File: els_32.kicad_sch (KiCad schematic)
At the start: 53 parts, among them J1 HR911105A, J2 JST-XH, J3 JST-XH, J4 Conn_01x03_Female, J5 WAGO, Q1 2N7002, Q2 Q_PMOS_DGS, U1 LAN8720A, U2 ESP32-WROOM-E, U3 MP2307, U4 LM3940

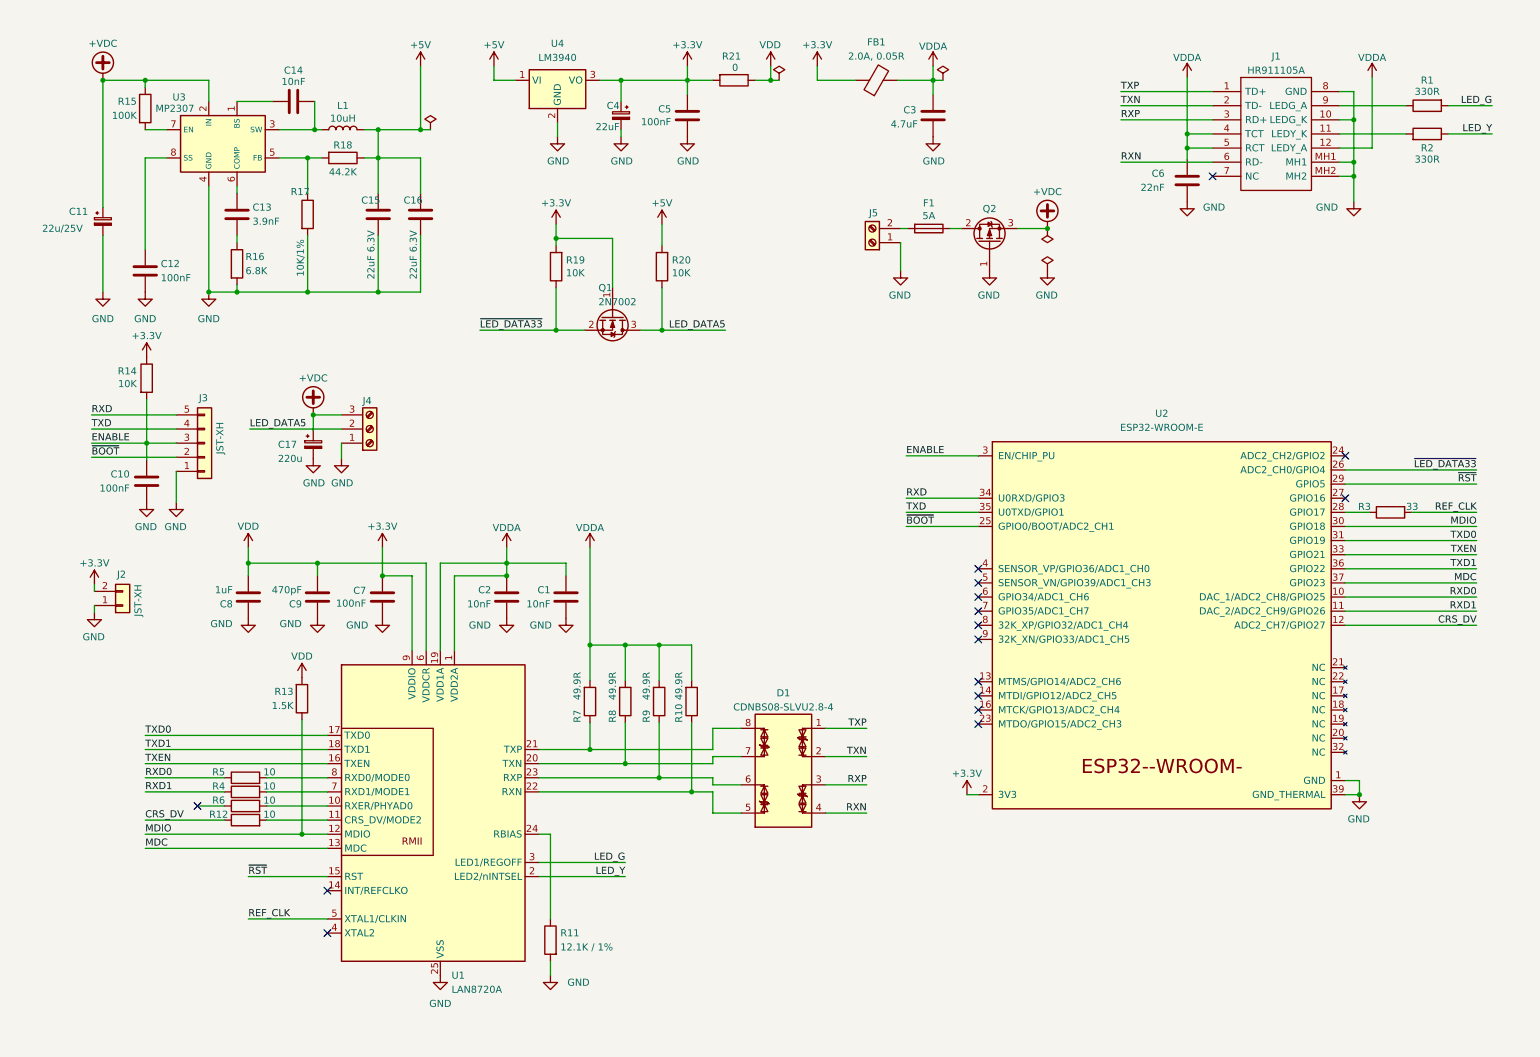
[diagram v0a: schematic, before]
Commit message: Update schematic: v0.2
- use TPS54321 for VDC -> 3.3V
- use 5.6 zener for level-shifting
- cleanup
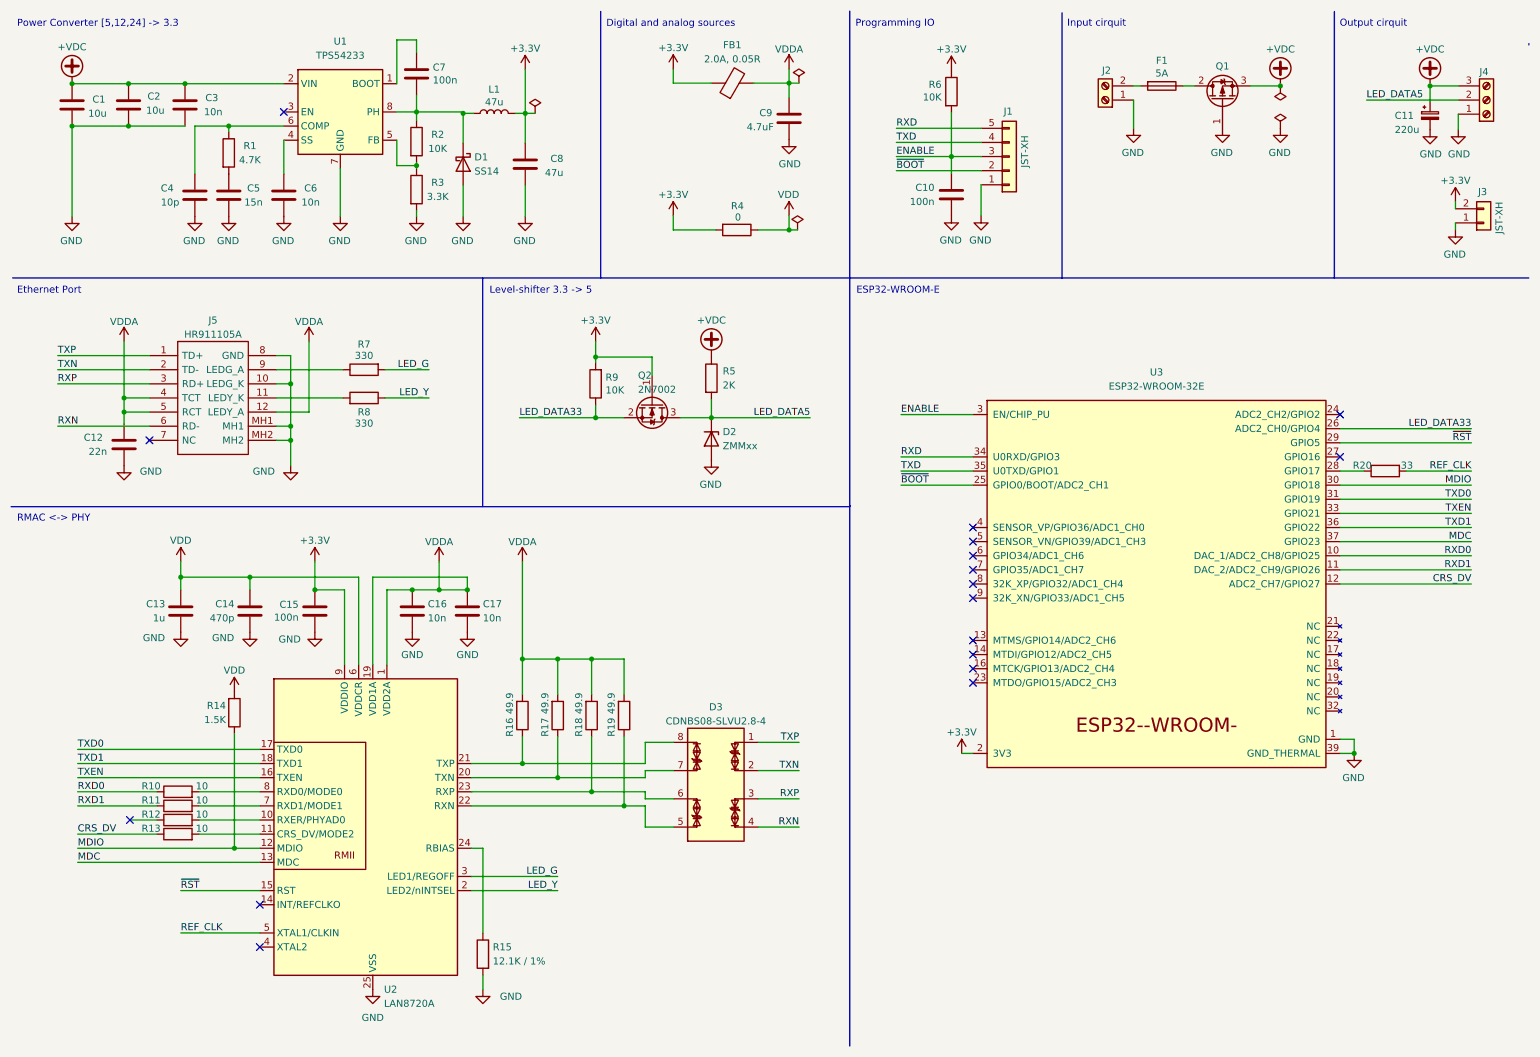
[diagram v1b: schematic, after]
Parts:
- removed C11: 22u/25V, Capacitor_SMD:C_0805_2012Metric, symbol Device:C_Polarized_Small
- removed C12: 100nF, Capacitor_SMD:C_0402_1005Metric, symbol Device:C
- removed C13: 3.9nF, Capacitor_SMD:C_0402_1005Metric, symbol Device:C
- removed C14: 10nF, Capacitor_SMD:C_0402_1005Metric, symbol Device:C
- removed C15, C16: 22uF 6.3V, Capacitor_SMD:C_0603_1608Metric, symbol Device:C
- removed C4: 22uF, Capacitor_Tantalum_SMD:CP_EIA-3528-21_Kemet-B, symbol Device:C_Polarized_Small
- removed R15: 100K, Resistor_SMD:R_0402_1005Metric, symbol Device:R
- removed R16: 6.8K, Resistor_SMD:R_0402_1005Metric, symbol Device:R
- removed R17: 10K/1%, Resistor_SMD:R_0402_1005Metric, symbol Device:R
- removed R18: 44.2K, Resistor_SMD:R_0402_1005Metric, symbol Device:R
- removed R20: 10K, Resistor_SMD:R_0402_1005Metric, symbol Device:R
- removed U3: MP2307, Package_SO:SOIC-8-1EP_3.9x4.9mm_P1.27mm_EP2.62x3.51mm, symbol MP2307:MP2307
- removed U4: LM3940, Package_TO_SOT_SMD:SOT-223-3_TabPin2, symbol LM3940:LM3940
- added C1, C2: 10u, Capacitor_SMD:C_1206_3216Metric, symbol Device:C
- added C3, C6: 10n, Capacitor_SMD:C_0402_1005Metric, symbol Device:C
- added C4: 10p, Capacitor_SMD:C_0603_1608Metric, symbol Device:C
- added C7: 100n, Capacitor_SMD:C_0402_1005Metric, symbol Device:C
- added C8: 47u, Capacitor_SMD:C_1206_3216Metric, symbol Device:C
- added D1: SS14, Diode_SMD:D_SMA, symbol Device:D_Schottky
- added D2: ZMMxx, Diode_SMD:D_MiniMELF, symbol Diode:ZMMxx
- added R1: 4.7K, Resistor_SMD:R_0402_1005Metric, symbol Device:R
- added R2: 10K, Resistor_SMD:R_0402_1005Metric, symbol Device:R
- added R3: 3.3K, Resistor_SMD:R_0402_1005Metric, symbol Device:R
- added R5: 2K, Resistor_SMD:R_1206_3216Metric, symbol Device:R
- added U1: TPS54233, Package_SO:SOIC-8_3.9x4.9mm_P1.27mm, symbol Regulator_Switching:TPS54233
- C10: value 100nF -> 100n
- C12: renamed from C6; value 22nF -> 22n
- C13: renamed from C8; value 1uF -> 1u
- C14: renamed from C9; value 470pF -> 470p
- C15: renamed from C7; value 100nF -> 100n
- C16: renamed from C2; value 10nF -> 10n
- C17: renamed from C1; value 10nF -> 10n
- C5: value 100nF -> 15n; footprint Capacitor_SMD:C_0402_1005Metric -> Capacitor_SMD:C_0603_1608Metric; LCSC C307331 -> C1596
- L1: value 10uH -> 47u; footprint Inductor_SMD:L_Sunlord_MWSA0518_5.4x5.2mm -> Inductor_SMD:L_Sunlord_MWSA06xxS; LCSC C181721 -> C408471
- R16: renamed from R7; value 49.9R -> 49.9
- R17: renamed from R8; value 49.9R -> 49.9
- R18: renamed from R9; value 49.9R -> 49.9
- R19: renamed from R10; value 49.9R -> 49.9
- R7: renamed from R1; value 330R -> 330
- R8: renamed from R2; value 330R -> 330
- U3: renamed from U2; value ESP32-WROOM-E -> ESP32-WROOM-32E; footprint Espressif:ESP32-WROOM-32E -> els_32-libs:ESP32-WROOM-32E
- renumbered C17 to C11, C3 to C9, D1 to D3, J3 to J1, J5 to J2, J2 to J3, J1 to J5, Q2 to Q1, Q1 to Q2, R5 to R10, R4 to R11, R6 to R12, R12 to R13, R13 to R14, R11 to R15, R3 to R20, R21 to R4, R14 to R6, R19 to R9, U1 to U2
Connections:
- net +5V is gone; now on net +3.3V: L1.2
- net +3.3V: now also C8.2; no longer C5.1
- net +VDC: now also C1.2, C2.1, C3.2, R5.1, U1.2 (VIN)
- net GND: now also C13.2, C14.2, C1.1, C2.2, C3.1, C4.1, C6.1, C8.1, D1.2 (A), D2.2 (A), R3.2, U1.7 (GND); no longer C13.1, C14.1
- net LED_DATA5: now also D2.1 (K), R5.2
- net VDD: now also C13.1, C14.1; no longer C13.2, C14.2
- net at L1.1: now also C7.2, D1.1 (K), R2.1, U1.8 (PH)
- net ~{LED_DATA33} renamed LED_DATA33
- new net: C4.2, R1.1, U1.6 (COMP)
- new net: R2.2, R3.1, U1.5 (FB)
- new net: C6.2, U1.4 (SS)
- new net: C5.1, R1.2
- new net: C7.1, U1.1 (BOOT)
- no-connect marks 16 -> 17
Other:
- note added: "Digital and analog sources"
- note added: "ESP32-WROOM-E"
- note added: "Ethernet Port"
- note added: "Input cirquit"
- note added: "Level-shifter 3.3 -> 5"
- note added: "Output cirquit"
- note added: "Power Converter [5,12,24] -> 3.3"
- note added: "Programming IO"
- note added: "RMAC <-> PHY"
- title: (none) -> ELS-32
- moved on the sheet: C10, C11, C12, C13, C14, C15, C16, C17, C9, D3, F1, FB1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

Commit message: update save
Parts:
- removed D2: ZMMxx, Diode_SMD:D_MiniMELF, symbol Diode:ZMMxx
- removed D3: CDNBS08-SLVU2.8-4, Package_SO:SOIC-8_3.9x4.9mm_P1.27mm, symbol Power_Protection:CDNBS08-SLVU2.8-4
- removed Q2: 2N7002, Package_TO_SOT_SMD:SOT-23, symbol Transistor_FET:BSS138
- removed R4: 0, Resistor_SMD:R_1206_3216Metric, symbol Device:R
- removed U3: ESP32-WROOM-32E, els_32-libs:ESP32-WROOM-32E, symbol Espressif:ESP32-WROOM-E
- added AE1: PCB_Ant, els_32-libs:ESPRESSIF_ESP32_MIFA_2.4GHz_Right, symbol PCB_ant:PCB_Ant
- added C12: 22u, Capacitor_SMD:C_1206_3216Metric, symbol Device:C
- added C13, C14, C23, C24, C28, C31, C32, C34, C35: 100n, Capacitor_SMD:C_0402_1005Metric, symbol Device:C
- added C21, C22: TBD, Capacitor_SMD:C_0402_1005Metric, symbol Device:C
- added C25: 10n, Capacitor_SMD:C_0402_1005Metric, symbol Device:C
- added C26, C27: 27p, Capacitor_SMD:C_0402_1005Metric, symbol Device:C
- added C29: 100p, Capacitor_SMD:C_0402_1005Metric, symbol Device:C
- added C30, C33: 1u, Capacitor_SMD:C_0402_1005Metric, symbol Device:C
- added C36: 10u, Capacitor_SMD:C_0603_1608Metric, symbol Device:C
- added D2, D3, D4, D5: ESD5Z5CL, Diode_SMD:D_SOD-523, symbol Device:D_TVS
- added L2: TBD, Inductor_SMD:L_0402_1005Metric, symbol Device:L
- added L3: 2n, Inductor_SMD:L_0402_1005Metric, symbol Device:L
- added R11: 2K, Resistor_SMD:R_0402_1005Metric, symbol Device:R
- added R12, R14: 33, Resistor_SMD:R_0402_1005Metric, symbol Device:R
- added R26, R27: 10, Resistor_SMD:R_0402_1005Metric, symbol Device:R
- added R28, R29: 4.7K, Resistor_SMD:R_0402_1005Metric, symbol Device:R
- added R30, R32, R6, R7, R8: 10K, Resistor_SMD:R_0402_1005Metric, symbol Device:R
- added R31: 10m, Resistor_SMD:R_1206_3216Metric, symbol Device:R_Shunt
- added R33: 510, Resistor_SMD:R_0402_1005Metric, symbol Device:R_Small
- added SW1, SW2: SW_MEC_5E, els_32-libs:TS1187ABAB, symbol Switch:SW_MEC_5E
- added U2: AZ1117-3.3, Package_TO_SOT_SMD:SOT-223-3_TabPin2, symbol Regulator_Linear:AZ1117-3.3
- added U3: SN74LVC2T45DCUR, Package_SO:VSSOP-8_2.4x2.1mm_P0.5mm, symbol Logic_LevelTranslator:SN74LVC2T45DCUR
- added U4: ESP32-D0WD-V3, Package_DFN_QFN:QFN-48-1EP_5x5mm_P0.35mm_EP3.7x3.7mm, symbol ESP32-D0WD-V3:ESP32-D0WD-V3
- added U6: INA226AIDGSR, Package_SO:MSOP-10_3x3mm_P0.5mm, symbol INA226AIDGSR:INA226AIDGSR
- added U7: W25Q32JVSS, Package_SO:SOIC-8_5.23x5.23mm_P1.27mm, symbol Memory_Flash:W25Q32JVSS
- added Y1: Crystal_GND24, Crystal:Crystal_SMD_2520-4Pin_2.5x2.0mm, symbol Device:Crystal_GND24
- C5: renamed from C9; value 4.7uF -> 4.7u
- F1: value 5A -> 10A
- J1: renamed from J2; value WAGO -> Conn_01x02_Female; footprint TerminalBlock_WAGO:TerminalBlock_WAGO_236-102_1x02_P5.00mm_45Degree -> els_32-libs:DBT50G-7.62-2P; LCSC (none) -> C496127
- J2: renamed from J4; value Conn_01x03_Female -> Conn_01x04_Female; footprint TerminalBlock_WAGO:TerminalBlock_WAGO_236-103_1x03_P5.00mm_45Degree -> els_32-libs:DBT50G-7.62-4P; symbol Connector:Screw_Terminal_01x03 -> Connector:Screw_Terminal_01x04; LCSC (none) -> C496132
- Q1: value Q_PMOS_DGS -> AONR21321; footprint Package_TO_SOT_SMD:SOT-23 -> els_32-libs:AONR21321; symbol Transistor_FET:SUD50P04-08 -> AONR21321:AONR21321; LCSC C20917 -> C541711
- R15: renamed from R20; symbol Device:R -> Device:R_Small
- R3: renamed from R1; value 4.7K -> 100; LCSC C25900 -> C25076
- R4: renamed from R3; value 3.3K -> 2K; LCSC C25890 -> C4109
- R5: value 2K -> 10K; footprint Resistor_SMD:R_1206_3216Metric -> Resistor_SMD:R_0402_1005Metric; LCSC C17944 -> C25744
- R9: value 10K -> 2K; LCSC C25744 -> C4109
- U1: value TPS54233 -> TPS54331
- renumbered C7 to C1, C6 to C10, C10 to C11, C12 to C15, C13 to C16, C14 to C17, C15 to C18, C16 to C19, C1 to C2, C17 to C20, C2 to C3, C3 to C4, C11 to C6, C8 to C7, C4 to C8, C5 to C9, J1 to J3, J3 to J4, R6 to R1, R7 to R10, R8 to R13, R14 to R16, R16 to R17, R17 to R18, R18 to R19, R19 to R20, R10 to R21, R11 to R22, R12 to R23, R13 to R24, R15 to R25, U2 to U5
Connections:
- net +3.3V: now also R16.2, R23.1, R5.2, C12.2, C24.2, C28.2, C29.2, C30.1, C31.2, C32.2, C35.2, C36.2, L3.2, R28.2, R29.2, R30.2, R32.2, R6.2, R7.2, R8.2, U2.2 (VO), U3.1 (VCCA), U4.1 (VDDA_1), U4.19 (VDD3P3_RTC), U4.37 (VDD3P3_CPU), U4.43 (VDDA_2), U4.46 (VDDA_3), U6.6 (VS); no longer C7.2, L1.2, R9.2
- net +VDC: now also Q1.1 (G), Q1.2 (G), R31.2; no longer C6.1, J2.3 (Pin_3), R5.1
- net CRS_DV: now also U4.16 (GPIO27)
- net ENABLE: now also U4.9 (CHIP_PU)
- net GND: now also J1.2 (Pin_2), J2.4 (Pin_4), Q1.4 (D), AE1.2, C12.1, C13.1, C14.1, C21.1, C22.1, C24.1, C25.1, C26.2, C27.2, C28.1, C29.1, C30.2, C31.1, C32.1, C33.2, C34.1, C35.1, C36.1, D2.2 (A2), D3.2 (A2), D4.2 (A2), D5.2 (A2), SW1.1, SW1.2, SW2.1, SW2.2, U2.1 (GND), U3.4 (GND), U4.49 (GND), U6.1 (A1), U6.2 (A0), U6.7 (GND), U7.4 (GND), Y1.2, Y1.4; no longer J1.1 (Pin_1), J2.1 (Pin_1), Q1.1 (G)
- net MDC: now also U4.36 (GPIO23)
- net MDIO: now also U4.35 (GPIO18)
- net RXD: now also U4.40 (U0RXD)
- net RXD0: now also U4.14 (GPIO25)
- net RXD1: now also U4.15 (GPIO26)
- net RXN: now also R20.1, U5.22 (RXN), D3.1 (A1)
- net RXP: now also R19.1, U5.23 (RXP), D4.1 (A1)
- net TXD: now also R33.2
- net TXD0: now also U4.38 (GPIO19)
- net TXD1: now also U4.39 (GPIO22)
- net TXEN: now also U4.42 (GPIO21)
- net TXN: now also R18.1, U5.20 (TXN), D2.1 (A1)
- net TXP: now also R17.1, U5.21 (TXP), D5.1 (A1)
- net ~{BOOT}: now also U4.23 (GPIO0)
- net ~{RST}: now also U4.34 (GPIO5)
- net at R15.1: now also U4.27 (GPIO17)
- net at F1.2: now also J1.1 (Pin_1); no longer J1.2 (Pin_2)
- net at C1.2, D1.1 (K), L1.1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: no longer R2.1
- net at F1.1: now also Q1.10 (S), Q1.11 (S), Q1.5 (S), Q1.6 (S), Q1.7 (S), Q1.8 (S), Q1.9 (S); no longer Q1.2 (D)
- net LED_DATA33: no longer names the net of R9.1
- net LED_DATA33: now also SW1.3 (K), SW1.4 (A)
- net LED_DATA5 renamed DATA2_50
- net DATA2_50: now also R14.2; no longer R5.2
- net VDD: no longer names the net of C16.1, C17.1, U5.6 (VDDCR)
- net VDD: no longer R16.2
- new net: C23.1, R27.2, U6.10 (IN+)
- new net: C23.2, R26.2, U6.9 (IN-)
- new net: AE1.1, C22.2, L2.1
- new net: C25.2, U4.48 (CAP1)
- new net: R32.1, U3.5 (DIR)
- new net: R12.1, U3.7 (B1)
- new net: C34.2, L3.1, U4.3 (VDD3P3_1), U4.4 (VDD3P3_2)
- new net: R33.1, U4.41 (U0TXD)
- new net: R14.1, U3.6 (B2)
- new net: R11.1, SW2.3 (K), SW2.4 (A)
- new net +5V: C7.2, L1.2, R2.1, U2.3 (VI), U3.8 (VCCB)
- new net ALERT: R30.1, U6.3 (ALERT)
- new net DATA1_33: R7.1, U3.2 (A1), U4.22 (GPIO2)
- new net DATA1_50: J2.3 (Pin_3), R12.2
- new net DATA2_33: R8.1, U3.3 (A2), U4.24 (GPIO4)
- new net FLASH_CLK: U4.31 (SD_CLK), U7.6 (CLK)
- new net FLASH_CS: U4.30 (SD_CMD), U7.1 (~{CS})
- new net FLASH_IO0: U4.32 (SD_DATA_0), U7.2 (DO(IO1))
- new net FLASH_IO1: U4.33 (SD_DATA_1), U7.5 (DI(IO0))
- new net FLASH_IO2: U4.28 (SD_DATA_2), U7.3 (IO2)
- new net FLASH_IO3: U4.29 (SD_DATA_3), U7.7 (IO3)
- new net FLASH_VDD: C33.1, U4.26 (VDD_SDIO), U7.8 (VCC)
- new net LNA_IN: C21.2, L2.2, U4.2 (LNA_IN)
- new net SCL: R28.1, U4.13 (32K_XN), U6.5 (SCL)
- new net SDA: R29.1, U4.12 (32K_XP), U6.4 (SDA)
- new net SHUNT+: R27.1, R31.2
- new net SHUNT-: C6.1, J2.1 (Pin_1), R26.1, R31.1, U6.8 (VBUS)
- new net USER0: C14.2, R11.2, R6.1, U4.20 (MTCK)
- new net USER1: C13.2, R5.1, R9.2, U4.17 (MTMS)
- new net XTAL_IN: C26.1, U4.45 (XTAL_P), Y1.1
- new net XTAL_OUT: C27.1, U4.44 (XTAL_N), Y1.3
- no-connect marks 17 -> 14
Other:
- added sheet ESP32 (esp32.kicad_sch)
- moved on the sheet: C1, C6, D1, J1, J4, L1, R15, R2, R4
